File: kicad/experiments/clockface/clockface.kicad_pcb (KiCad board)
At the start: 2 copper layers, 11 parts, among them P1 BATTERY, U1 TOUCH_PAD_13, U2 MTCH6102_SSOP

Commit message: RX traces
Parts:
- P1: value BATTERY -> CONN_01X05; footprint Resistors_SMD:R_0805_HandSoldering -> Pin_Headers:Pin_Header_Straight_1x06
- moved C2 21.2 mm to (166.1, 89.4), turned to 0 degrees
- moved C1 9.86 mm to (158.5, 92.5)
- moved P1 7.15 mm to (141.2, 59.9), turned to 270 degrees
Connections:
- net VCC renamed /3V3
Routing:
- net /RX8: track 5.63 -> 34.9 mm
- net GND: track 0.00 -> 29.0 mm
- net /RX7: track 5.65 -> 30.9 mm
- net /RX11: track 5.61 -> 28.9 mm
- net /RX6: track 5.22 -> 26.6 mm
- net /RX10: track 5.64 -> 23.5 mm
- net /RX5: track 5.66 -> 22.1 mm
- net /3V3: track 0.00 -> 15.8 mm
- net /RX0: track 5.27 -> 21.0 mm
- net /RX3: track 5.28 -> 19.9 mm
- net /RX12: track 0.00 -> 14.1 mm
- net /RX4: track 5.62 -> 19.4 mm
- net /RX1: track 5.68 -> 18.3 mm
- net /RX2: track 5.67 -> 18.2 mm
- net /RX9: track 5.25 -> 17.7 mm

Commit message: Layed out
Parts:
- P1: footprint Pin_Headers:Pin_Header_Straight_1x06 -> clockface:SMD_Header_Straight_1x05
- moved R4 28.5 mm to (133.9, 72.3)
- moved R3 27.0 mm to (131.4, 72.3)
- moved R5 25.5 mm to (128.8, 72.3)
- moved P1 16.9 mm to (136.4, 76.2), turned to 90 degrees
- moved D1 15.6 mm to (147.9, 71.1)
- moved R1 15.6 mm to (142.8, 71.1)
- moved R2 0.75 mm to (142.8, 101.0)
- moved C1 0.49 mm to (158.7, 92.9)
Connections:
- P1 pad 1: GND -> /3V3
- P1 pad 2: /3V3 -> /SCL
- P1 pad 4: /SCL -> /INT
- P1 pad 5: /INT -> GND
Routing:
- net GND: track 29.0 -> 200.5 mm
- net /3V3: track 15.8 -> 88.1 mm
- net /INT: track 0.00 -> 37.5 mm
- net /SDA: track 0.00 -> 34.3 mm
- net /SCL: track 0.00 -> 32.3 mm
- net Net-(R2-Pad2): track 0.00 -> 5.15 mm
- net Net-(D1-Pad2): track 0.00 -> 2.68 mm
- net /RX0: track 21.0 -> 22.7 mm
- added copper zone on B.Cu, net GND
- added copper zone on F.Cu, net GND
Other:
- board outline added: 50 x 50 mm
- board text added: "-"
- board text added: "0"
- board text added: "1"
- board text added: "2"
- board text added: "3"
- board text added: "4"
- board text added: "5"
- board text added: "6"
- board text added: "7"
- board text added: "9"

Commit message: Numbers on the keys
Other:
- board text added: "8"
- board text added: "="
- board text added: ">"
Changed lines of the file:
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@@
     (area 122.741999 68.527999 172.892001 118.678001)
     (thickness 1.6)
-    (drawings 17)
+    (drawings 19)
     (tracks 189)
     (zones 0)
@@
     (pad 2 thru_hole circle (at 7.1882 -12.8016) (size 0.75 0.75) (drill 0.4) (layers *.Cu *.Mask)
       (net 17 /RX1))
-    (pad 13 smd circle (at 0 0) (size 15 15) (layers F.Cu F.Mask)
+    (pad 13 smd circle (at 0 0) (size 15 15) (layers F.Cu)
       (net 18 /RX12))
-    (pad 1 smd circle (at 0 -20) (size 8 8) (layers F.Cu F.Mask)
+    (pad 1 smd circle (at 0 -20) (size 8 8) (layers F.Cu)
       (net 19 /RX0))
-    (pad 2 smd circle (at 9.999999 -17.320508) (size 8 8) (layers F.Cu F.Mask)
+    (pad 2 smd circle (at 9.999999 -17.320508) (size 8 8) (layers F.Cu)
       (net 17 /RX1))
-    (pad 3 smd circle (at 17.320508 -10) (size 8 8) (layers F.Cu F.Mask)
+    (pad 3 smd circle (at 17.320508 -10) (size 8 8) (layers F.Cu)
       (net 16 /RX2))
-    (pad 4 smd circle (at 20 0) (size 8 8) (layers F.Cu F.Mask)
+    (pad 4 smd circle (at 20 0) (size 8 8) (layers F.Cu)
       (net 15 /RX3))
-    (pad 5 smd circle (at 17.320508 9.999999) (size 8 8) (layers F.Cu F.Mask)
+    (pad 5 smd circle (at 17.320508 9.999999) (size 8 8) (layers F.Cu)
       (net 14 /RX4))
-    (pad 6 smd circle (at 9.999999 17.320508) (size 8 8) (layers F.Cu F.Mask)
+    (pad 6 smd circle (at 9.999999 17.320508) (size 8 8) (layers F.Cu)
       (net 13 /RX5))
-    (pad 7 smd circle (at 0 20) (size 8 8) (layers F.Cu F.Mask)
+    (pad 7 smd circle (at 0 20) (size 8 8) (layers F.Cu)
       (net 12 /RX6))
-    (pad 8 smd circle (at -10 17.320508) (size 8 8) (layers F.Cu F.Mask)
+    (pad 8 smd circle (at -10 17.320508) (size 8 8) (layers F.Cu)
       (net 11 /RX7))
-    (pad 9 smd circle (at -17.320508 10) (size 8 8) (layers F.Cu F.Mask)
+    (pad 9 smd circle (at -17.320508 10) (size 8 8) (layers F.Cu)
       (net 10 /RX8))
-    (pad 10 smd circle (at -20 0) (size 8 8) (layers F.Cu F.Mask)
+    (pad 10 smd circle (at -20 0) (size 8 8) (layers F.Cu)
       (net 9 /RX9))
-    (pad 11 smd circle (at -17.320508 -10) (size 8 8) (layers F.Cu F.Mask)
+    (pad 11 smd circle (at -17.320508 -10) (size 8 8) (layers F.Cu)
       (net 8 /RX10))
-    (pad 12 smd circle (at -10 -17.320508) (size 8 8) (layers F.Cu F.Mask)
+    (pad 12 smd circle (at -10 -17.320508) (size 8 8) (layers F.Cu)
       (net 7 /RX11))
     (pad 1 thru_hole circle (at 0 -14.732) (size 0.75 0.75) (drill 0.4) (layers *.Cu *.Mask)
@@
       (net 1 GND))
   )
+  (gr_text = (at 149.96414 93.99524 90) (layer F.Mask)
+    (effects (font (size 3 3) (thickness 0.7)))
+  )
+  (gr_text > (at 146.78914 93.80474) (layer F.Mask)
+    (effects (font (size 3 3) (thickness 0.7)))
+  )
   (gr_line (start 137.77214 76.78674) (end 137.77214 73.23074) (angle 90) (layer F.Mask) (width 0.5))
   (gr_circle (center 137.77214 76.59624) (end 139.48664 75.26274) (layer F.Mask) (width 0.5))
@@
     (effects (font (size 3 3) (thickness 0.5)))
   )
-  (gr_text 9 (at 130.46964 103.90124) (layer F.Mask)
+  (gr_text 8 (at 130.46964 103.90124) (layer F.Mask)
     (effects (font (size 3 3) (thickness 0.5)))
   )

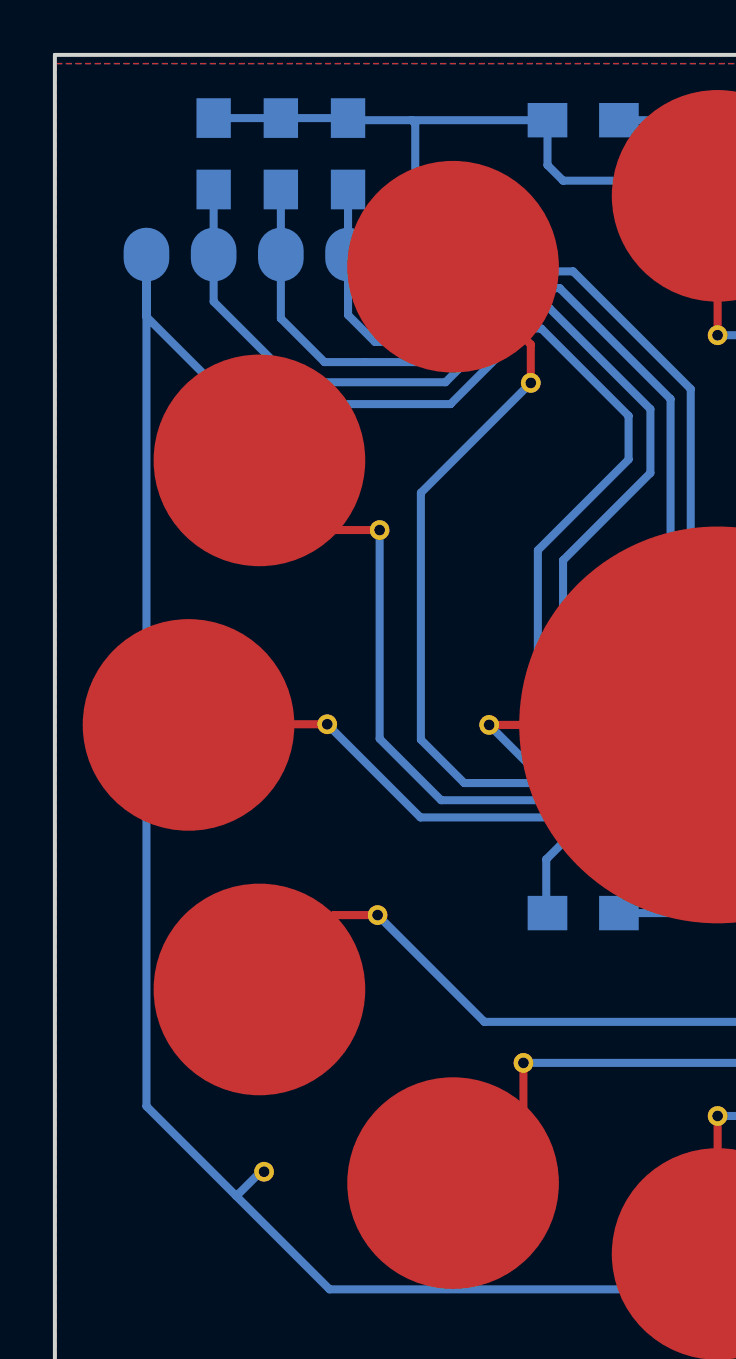
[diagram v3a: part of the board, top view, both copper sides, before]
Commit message: Moved header closer to the edge
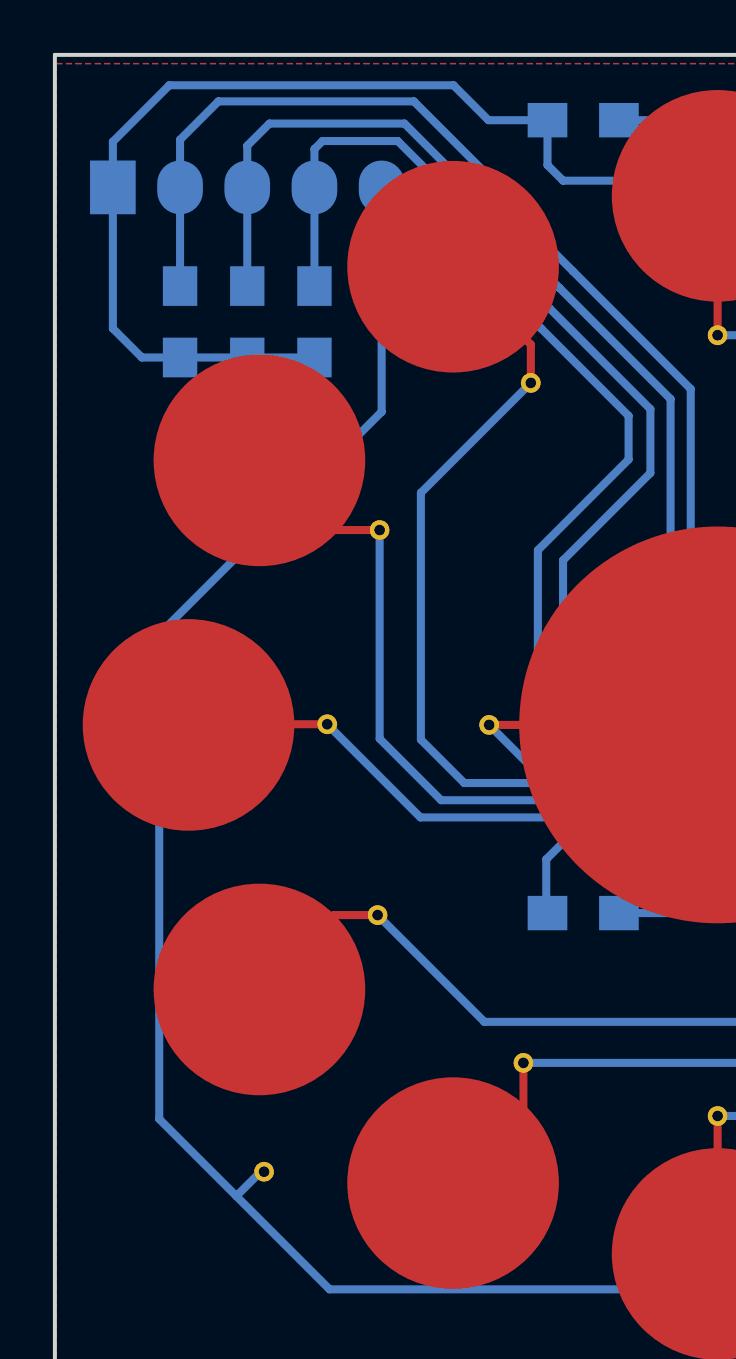
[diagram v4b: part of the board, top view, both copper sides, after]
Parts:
- moved P1 11.7 mm to (125.0, 73.6), turned to 270 degrees
- moved R4 8.98 mm to (127.5, 78.7), turned to 90 degrees
- moved R5 7.41 mm to (132.6, 78.7), turned to 90 degrees
- moved R3 6.48 mm to (130.1, 78.7), turned to 90 degrees
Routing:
- net /3V3: track 88.1 -> 103.3 mm
- net /SCL: track 32.3 -> 41.5 mm
- net GND: track 200.5 -> 194.7 mm
- net /INT: track 37.5 -> 35.3 mm
- net /SDA: track 34.3 -> 36.4 mm
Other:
- board text added: "3v3"
- board text added: "GND"
- board text added: "INT"
- board text added: "SCL"
- board text added: "SDA"

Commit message: Changed layout
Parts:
- moved R5 28.8 mm to (147.7, 103.2), turned to 180 degrees
- moved C2 21.4 mm to (150.2, 75.1), turned to 270 degrees
- moved R4 20.9 mm to (147.9, 83.5), turned to 180 degrees
- moved R3 19.3 mm to (147.9, 86.3), turned to 180 degrees
- moved R1 19.3 mm to (161.7, 75.0), turned to 270 degrees
- moved D1 18.8 mm to (166.3, 74.8)
- moved P1 12.7 mm to (137.7, 73.6), turned to 90 degrees
- moved R2 4.96 mm to (147.7, 100.8)
- moved C1 0.63 mm to (158.0, 92.9)
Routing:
- net GND: track 194.7 -> 209.6 mm
- net /INT: track 35.3 -> 48.7 mm
- net /3V3: track 103.3 -> 91.7 mm
- net /SCL: track 41.5 -> 33.3 mm
- net /SDA: track 36.4 -> 30.7 mm
- net Net-(D1-Pad2): track 2.68 -> 4.19 mm
- net Net-(R2-Pad2): track 5.15 -> 4.50 mm

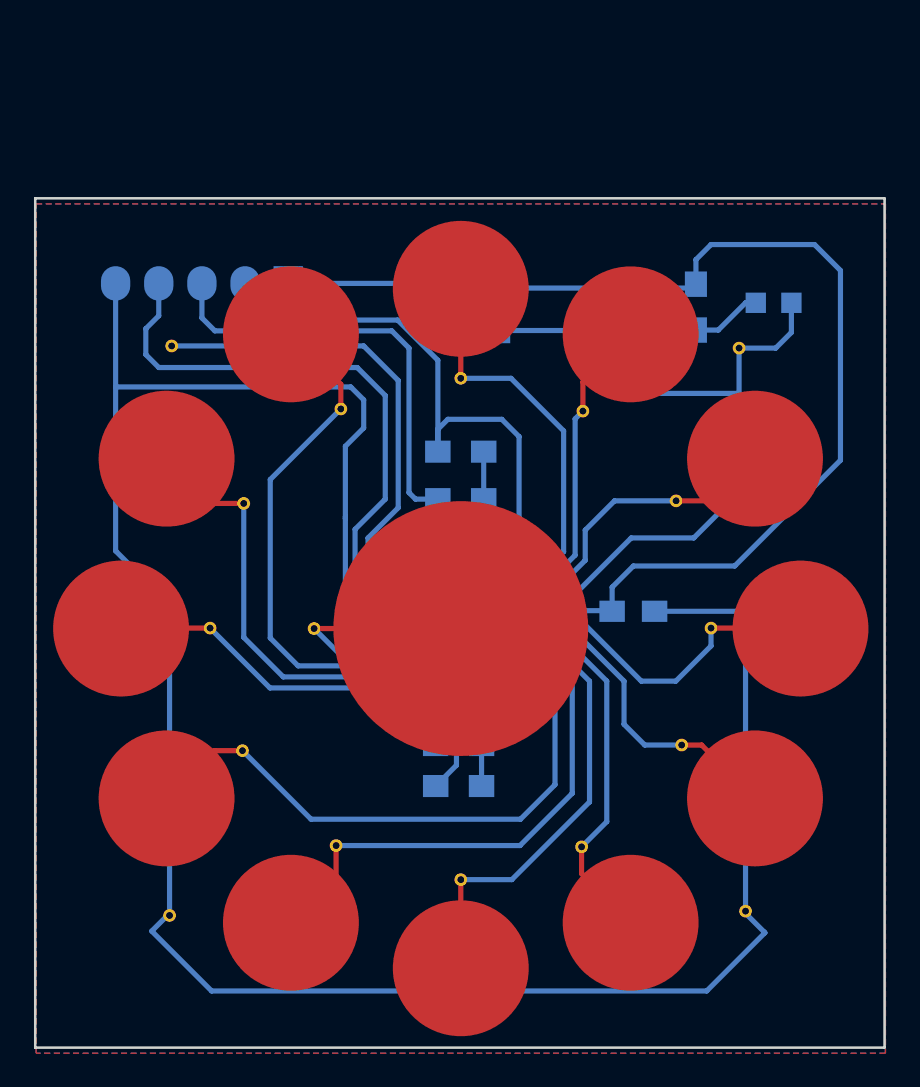
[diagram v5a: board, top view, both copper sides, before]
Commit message: Vias not holes in the touch footprint
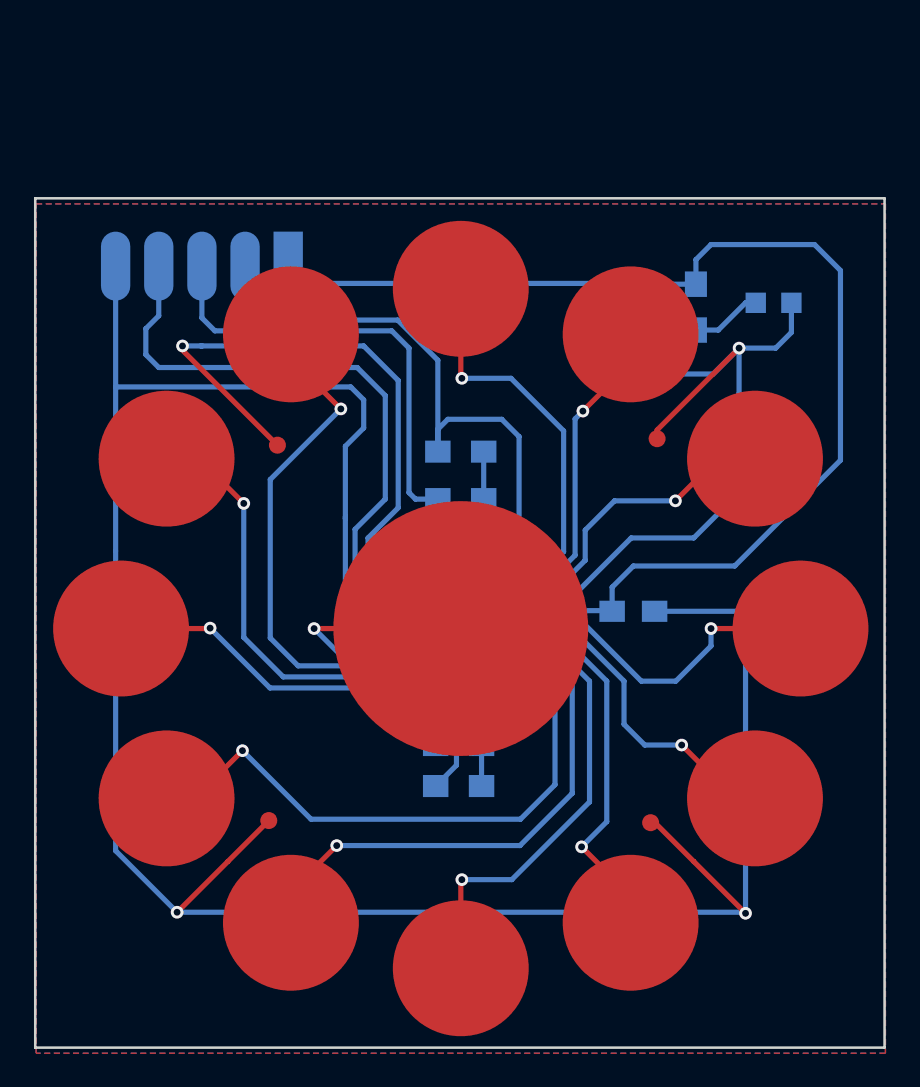
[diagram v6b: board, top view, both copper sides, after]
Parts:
- P1: footprint clockface:SMD_Header_Straight_1x05 -> SMD_Header_Straight_1x05
- moved C2 8.39 mm to (158.5, 74.9)
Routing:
- net GND: track 209.6 -> 224.3 mm, vias 0 -> 4
- net /RX2: vias 0 -> 1
- net /RX9: vias 0 -> 1
- net /RX6: vias 0 -> 1
- net /RX0: vias 0 -> 1
- net /RX3: track 19.9 -> 20.0 mm, vias 0 -> 1
- net /RX7: vias 0 -> 1
- net /RX10: vias 0 -> 1
- net /RX12: vias 0 -> 1
- net /RX4: vias 0 -> 1
- net /RX5: vias 0 -> 1
- net /RX8: vias 0 -> 1
- net /RX11: vias 0 -> 1
- net /RX1: vias 0 -> 1

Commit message: tweaks
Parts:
- moved C2 18.9 mm to (167.2, 91.6)
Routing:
- net GND: track 224.3 -> 219.7 mm
- net /3V3: track 91.9 -> 94.8 mm
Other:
- board text added: "https://github.com/theapi/touch_timer kicad/experiments/clockface v1.0"

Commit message: tweaks
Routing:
- net /RX0: track 22.7 -> 21.8 mm
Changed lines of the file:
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@@
     (visible_elements 7FFFF7FF)
     (pcbplotparams
-      (layerselection 0x00030_80000001)
-      (usegerberextensions false)
+      (layerselection 0x01030_80000001)
+      (usegerberextensions true)
+      (usegerberattributes true)
       (excludeedgelayer true)
       (linewidth 0.100000)
@@
       (plotinvisibletext false)
       (padsonsilk false)
-      (subtractmaskfromsilk false)
+      (subtractmaskfromsilk true)
       (outputformat 1)
       (mirror false)
-      (drillshape 1)
+      (drillshape 0)
       (scaleselection 1)
-      (outputdirectory ""))
+      (outputdirectory gerber/))
   )
   (net 0 "")
@@
       (effects (font (size 1 1) (thickness 0.15)) (justify mirror))
     )
-    (fp_text value 0.1uF (at 0 -2.1) (layer B.Fab)
+    (fp_text value 0.1uF (at -0.127 -2.159) (layer B.SilkS)
       (effects (font (size 1 1) (thickness 0.15)) (justify mirror))
     )
@@
     (tags "capacitor 0805")
     (attr smd)
-    (fp_text reference C2 (at 0 2.032 360) (layer B.SilkS)
-      (effects (font (size 1 1) (thickness 0.15)) (justify mirror))
-    )
-    (fp_text value 10uF (at 0 -2.1 270) (layer B.Fab)
+    (fp_text reference C2 (at -0.508 2.159 360) (layer B.SilkS)
+      (effects (font (size 1 1) (thickness 0.15)) (justify mirror))
+    )
+    (fp_text value 10uF (at 1.016 3.048 360) (layer B.SilkS)
       (effects (font (size 1 1) (thickness 0.15)) (justify mirror))
     )
@@
     )
   )
-  (gr_text "https://github.com/theapi/touch_timer\nkicad/experiments/clockface  v1.0" (at 147.74164 113.36274) (layer B.SilkS)
+  (gr_text "https://github.com/theapi/touch_timer\nkicad/experiments/clockface v1.0" (at 147.74164 113.36274) (layer B.SilkS)
     (effects (font (size 1 1) (thickness 0.15) italic) (justify mirror))
   )
@@
   (segment (start 153.532 91.578) (end 155.194 89.916) (width 0.305) (layer B.Cu) (net 16))
   (via (at 155.057201 81.1294) (size 0.75) (drill 0.4) (layers F.Cu B.Cu) (net 17))
-  (segment (start 153.28538 90.928) (end 154.59964 89.61374) (width 0.305) (layer B.Cu) (net 17))
-  (segment (start 154.59964 89.61374) (end 154.59964 81.586961) (width 0.305) (layer B.Cu) (net 17))
-  (segment (start 154.59964 81.586961) (end 155.057201 81.1294) (width 0.305) (layer B.Cu) (net 17))
+  (segment (start 153.28538 90.928) (end 154.09164 90.12174) (width 0.305) (layer B.Cu) (net 17))
+  (segment (start 154.09164 90.12174) (end 154.09164 82.094961) (width 0.305) (layer B.Cu) (net 17))
+  (segment (start 154.09164 82.094961) (end 155.057201 81.1294) (width 0.305) (layer B.Cu) (net 17))
   (segment (start 151.301 90.928) (end 153.28538 90.928) (width 0.305) (layer B.Cu) (net 17))
   (segment (start 155.057201 81.1294) (end 157.869 78.317601) (width 0.305) (layer F.Cu) (net 17))
@@
   (segment (start 147.869001 73.931) (end 147.869001 79.135861) (width 0.305) (layer F.Cu) (net 19))
   (segment (start 147.869001 79.135861) (end 147.93214 79.199) (width 0.305) (layer F.Cu) (net 19))
-  (segment (start 151.301 90.278) (end 153.054 90.278) (width 0.305) (layer B.Cu) (net 19))
+  (segment (start 151.301 90.278) (end 152.8 90.278) (width 0.305) (layer B.Cu) (net 19) (status 400000))
   (segment (start 150.827 79.199) (end 147.93214 79.199) (width 0.305) (layer B.Cu) (net 19))
   (segment (start 147.93214 79.199) (end 147.869001 79.199) (width 0.305) (layer B.Cu) (net 19))
-  (segment (start 153.924 82.296) (end 150.827 79.199) (width 0.305) (layer B.Cu) (net 19))
-  (segment (start 153.924 89.408) (end 153.924 82.296) (width 0.305) (layer B.Cu) (net 19))
-  (segment (start 153.054 90.278) (end 153.924 89.408) (width 0.305) (layer B.Cu) (net 19))
+  (segment (start 153.035 81.407) (end 150.827 79.199) (width 0.305) (layer B.Cu) (net 19))
+  (segment (start 153.035 90.043) (end 153.035 81.407) (width 0.305) (layer B.Cu) (net 19))
+  (segment (start 152.8 90.278) (end 153.035 90.043) (width 0.305) (layer B.Cu) (net 19))
   (segment (start 167.17264 90.39574) (end 168.87984 90.39574) (width 0.305) (layer B.Cu) (net 26))
   (segment (start 170.22064 87.32774) (end 170.22064 84.02574) (width 0.305) (layer B.Cu) (net 26))
